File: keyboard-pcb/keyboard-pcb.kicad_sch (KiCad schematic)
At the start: 57 parts, among them SW1 SW_Push, SW10 SW_Push, SW11 SW_Push, SW12 SW_Push, SW13 SW_Push, SW14 SW_Push, SW15 SW_Push, SW16 SW_Push, SW17 SW_Push, SW18 SW_Push, SW19 SW_Push, SW2 SW_Push, SW20 SW_Push, SW21 SW_Push, SW22 SW_Push, SW23 SW_Push, SW24 SW_Push, SW25 SW_Push, SW26 SW_Push, SW27 SW_Push, SW28 SW_Push, SW3 SW_Push, SW4 SW_Push, SW5 SW_Push, SW6 SW_Push, SW7 SW_Push, SW8 SW_Push, SW9 SW_Push, U1 RC1602A

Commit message: placement in progress
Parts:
- removed D28: 1N914, Diode_THT:D_DO-35_SOD27_P7.62mm_Horizontal, symbol Diode:1N914
- removed SW28: SW_Push, Button_Switch_Keyboard:SW_Cherry_MX_1.00u_PCB, symbol Switch:SW_Push
- added U1: ATmega328-P, Package_DIP:DIP-28_W7.62mm, symbol MCU_Microchip_ATmega:ATmega328-P
- renumbered U1 to U2
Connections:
- net GND: now reaches U2.1 (VSS)
- net GND: now also U2.5 (R/W), U1.22 (GND), U1.8 (GND)
- net VCC: now reaches U2.2 (VDD)
- net VCC: now also U1.20 (AVCC), U1.7 (VCC)
- net ROW4: now reaches SW17.1, SW18.1, SW19.1, SW20.1
- net ROW4: now also U1.6 (PD4)
- net ROW5: now reaches SW21.1, SW22.1, SW23.1, SW24.1
- net ROW5: now also U1.11 (PD5)
- net COL1: now reaches D10.1 (K), D14.1 (K), D18.1 (K), D2.1 (K), D22.1 (K), D26.1 (K), D6.1 (K)
- net COL1: now also U1.27 (PC4)
- net ROW3: now reaches SW13.1, SW14.1, SW15.1, SW16.1
- net ROW3: now also U1.5 (PD3)
- net COL2: now reaches D11.1 (K), D15.1 (K), D19.1 (K), D23.1 (K), D27.1 (K), D3.1 (K), D7.1 (K)
- net COL2: now also U1.28 (PC5)
- net COL0: now reaches D1.1 (K), D13.1 (K), D17.1 (K), D21.1 (K), D25.1 (K), D5.1 (K), D9.1 (K)
- net COL0: now also U1.16 (PB2)
- net ROW0: now reaches SW1.1, SW2.1, SW3.1, SW4.1
- net ROW0: now also U1.2 (PD0)
- net ROW1: now reaches SW5.1, SW6.1, SW7.1, SW8.1
- net ROW1: now also U1.3 (PD1)
- net COL3: now reaches D12.1 (K), D16.1 (K), D20.1 (K), D24.1 (K), D4.1 (K), D8.1 (K)
- net COL3: now also U1.13 (PD7)
- net ROW2: now reaches SW10.1, SW11.1, SW12.1, SW9.1
- net ROW2: now also U1.4 (PD2)
- net ROW6: now reaches SW25.1, SW26.1, SW27.1
- net ROW6: now also U1.12 (PD6)
- new net D0: U1.23 (PC0)
- new net D1: U1.24 (PC1)
- new net D2: U1.25 (PC2)
- new net D3: U1.26 (PC3)
- new net EN: U1.9 (XTAL1/PB6)
- new net MISO: U1.18 (PB4)
- new net MOSI: U1.17 (PB3)
- new net RS: U1.10 (XTAL2/PB7)
- new net SCK: U1.19 (PB5)
- new net nRST: U1.1 (~{RESET}/PC6)
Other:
- company: (none) -> UPCO Graphics Systems
- title: (none) -> Hex Calculator
- moved on the sheet: D1, D10, D11, D12, D13, D14, D15, D16, D17, D18, D19, D2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

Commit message: placement
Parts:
- added R1: R, Resistor_THT:R_Axial_DIN0207_L6.3mm_D2.5mm_P7.62mm_Horizontal, symbol Device:R
- added RV1: R_Potentiometer, Potentiometer_THT:Potentiometer_Bourns_3266P_Horizontal, symbol Device:R_Potentiometer
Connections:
- net D0: now also U2.11 (DB4)
- net D1: now also U2.12 (DB5)
- net D2: now also U2.13 (DB6)
- net D3: now also U2.14 (DB7)
- net EN: now also U2.6 (E)
- net GND: now also U2.10 (DB3), U2.7 (DB0), U2.8 (DB1), U2.9 (DB2), R1.2, RV1.3
- net RS: now also U2.4 (RS)
- net VCC: now also U2.15 (A/VEE), RV1.1
- net at U2.16 (K): now also R1.1
- net at U2.3 (VO): now also RV1.2

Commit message: working on placement
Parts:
- added BT1: 2xAAA, symbol Device:Battery
- added C1, C3: 0.1uF, Capacitor_SMD:C_0805_2012Metric_Pad1.18x1.45mm_HandSolder, symbol Device:C
- added C2: 10uF, Capacitor_SMD:C_0805_2012Metric_Pad1.18x1.45mm_HandSolder, symbol Device:C
- added D1, D11, D2: LED, LED_THT:LED_D3.0mm, symbol Device:LED
- added J1: Conn_02x03_Odd_Even, Connector_PinHeader_2.54mm:PinHeader_2x03_P2.54mm_Vertical, symbol Connector_Generic:Conn_02x03_Odd_Even
- added R1, R2, R3: 470, Resistor_THT:R_Axial_DIN0207_L6.3mm_D2.5mm_P7.62mm_Horizontal, symbol Device:R
- added R4: 10k, Resistor_THT:R_Axial_DIN0207_L6.3mm_D2.5mm_P7.62mm_Horizontal, symbol Device:R
- added SW5: SW_SPST, Connector_PinHeader_2.54mm:PinHeader_1x02_P2.54mm_Vertical, symbol Switch:SW_SPST
- added U1: R1500H, Package_TO_SOT_SMD:SOT-89-5_Handsoldering, symbol R1500H_vreg:R1500H
- R5: renamed from R1; value R -> 470
- RV1: value R_Potentiometer -> 10k
- renumbered D8 to D10, D9 to D12, D10 to D13, D11 to D14, D12 to D15, D13 to D16, D14 to D17, D15 to D18, D16 to D19, D17 to D20, D18 to D21, D19 to D22, D20 to D23, D21 to D24, D22 to D25, D23 to D26, D24 to D27, D25 to D28, D26 to D29, D1 to D3, D27 to D30, D2 to D4, D3 to D5, D4 to D6, D5 to D7, D6 to D8, D7 to D9, SW9 to SW10, SW10 to SW11, SW11 to SW12, SW12 to SW13, SW13 to SW14, SW14 to SW15, SW15 to SW16, SW16 to SW17, SW17 to SW18, SW18 to SW19, SW19 to SW20, SW20 to SW21, SW21 to SW22, SW22 to SW23, SW23 to SW24, SW24 to SW25, SW25 to SW26, SW26 to SW27, SW27 to SW28, SW5 to SW6, SW6 to SW7, SW7 to SW8, SW8 to SW9, U1 to U2, U2 to U3
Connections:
- net GND: now also BT1.2 (-), C1.2, C2.2, C3.2, D11.1 (K), J1.6 (Pin_6), U1.2 (GND), U1.3 (GND)
- net MISO: now also J1.1 (Pin_1)
- net MOSI: now also J1.4 (Pin_4)
- net SCK: now also J1.3 (Pin_3)
- net VCC: now also C1.1, C2.1, J1.2 (Pin_2), R1.1, R2.1, R3.1, R4.1, U1.5 (VOUT)
- net nRST: now also J1.5 (Pin_5), R4.2
- net at U2.14 (PB0): now also D1.1 (K)
- net at U2.15 (PB1): now also D2.1 (K)
- new net: C3.1, SW5.1 (A), U1.1 (VIN), U1.4 (CE)
- new net: D11.2 (A), R3.2
- new net: D2.2 (A), R2.2
- new net: BT1.1 (+), SW5.2 (B)
- new net: D1.2 (A), R1.2

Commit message: starting software
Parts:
- BT1: footprint (none) -> Battery:BatteryHolder_Keystone_2468_2xAAA
- C1, C2, C3: footprint Capacitor_SMD:C_0805_2012Metric_Pad1.18x1.45mm_HandSolder -> Capacitor_THT:C_Disc_D5.0mm_W2.5mm_P2.50mm
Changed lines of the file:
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@@
       (effects (font (size 1.27 1.27)) (justify left))
     )
-    (property "Footprint" "Capacitor_SMD:C_0805_2012Metric_Pad1.18x1.45mm_HandSolder" (at 219.4052 68.58 0)
+    (property "Footprint" "Capacitor_THT:C_Disc_D5.0mm_W2.5mm_P2.50mm" (at 219.4052 68.58 0)
       (effects (font (size 1.27 1.27)) hide)
     )
@@
       (effects (font (size 1.27 1.27)) (justify left))
     )
-    (property "Footprint" "Capacitor_SMD:C_0805_2012Metric_Pad1.18x1.45mm_HandSolder" (at 256.2352 66.04 0)
+    (property "Footprint" "Capacitor_THT:C_Disc_D5.0mm_W2.5mm_P2.50mm" (at 256.2352 66.04 0)
       (effects (font (size 1.27 1.27)) hide)
     )
@@
       (effects (font (size 1.27 1.27)) (justify left))
     )
-    (property "Footprint" "" (at 204.47 63.246 90)
+    (property "Footprint" "Battery:BatteryHolder_Keystone_2468_2xAAA" (at 204.47 63.246 90)
       (effects (font (size 1.27 1.27)) hide)
     )
@@
       (effects (font (size 1.27 1.27)) (justify left))
     )
-    (property "Footprint" "Capacitor_SMD:C_0805_2012Metric_Pad1.18x1.45mm_HandSolder" (at 27.6352 27.94 0)
-      (effects (font (size 1.27 1.27)) hide)
-    )
+    (property "Footprint" "Capacitor_THT:C_Disc_D5.0mm_W2.5mm_P2.50mm" (at 27.6352 27.94 0)
+      (effects (font (size 1.27 1.27)) hide)
+    )

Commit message: placement done?
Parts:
- SW5: footprint Connector_PinHeader_2.54mm:PinHeader_1x02_P2.54mm_Vertical -> my_switch:ANT11TFHQE_switch; CatNo (none) -> 2449-ANT11TFHQE-ND
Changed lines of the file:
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@@
   )
   (symbol (lib_id "Switch:SW_SPST") (at 210.82 54.61 0) (mirror y) (unit 1)
-    (in_bom yes) (on_board yes) (dnp no) (fields_autoplaced)
-    (property "Reference" "SW5" (at 210.82 49.53 0)
+    (in_bom yes) (on_board yes) (dnp no)
+    (property "Reference" "SW5" (at 205.74 50.8 0)
       (effects (font (size 1.27 1.27)))
     )
-    (property "Value" "SW_SPST" (at 210.82 52.07 0)
+    (property "Value" "SW_SPST" (at 214.63 50.8 0)
       (effects (font (size 1.27 1.27)))
     )
-    (property "Footprint" "Connector_PinHeader_2.54mm:PinHeader_1x02_P2.54mm_Vertical" (at 210.82 54.61 0)
+    (property "Footprint" "my_switch:ANT11TFHQE_switch" (at 210.82 54.61 0)
       (effects (font (size 1.27 1.27)) hide)
     )
@@
       (effects (font (size 1.27 1.27)) hide)
     )
+    (property "CatNo" "2449-ANT11TFHQE-ND" (at 210.82 48.26 0)
+      (effects (font (size 1.27 1.27)))
+    )
     (pin "1")

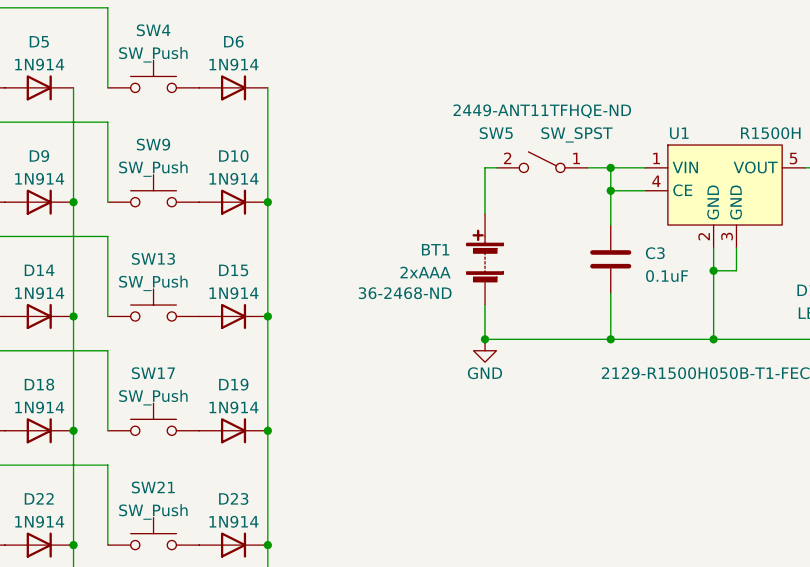
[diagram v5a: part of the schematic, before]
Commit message: change to AAA, software updates
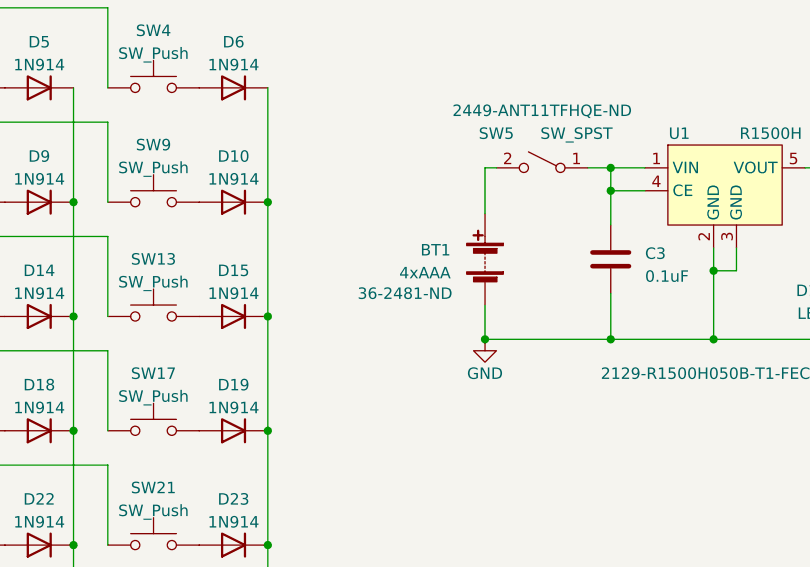
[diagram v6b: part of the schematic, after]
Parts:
- BT1: value 2xAAA -> 4xAAA; footprint Battery:BatteryHolder_Keystone_2468_2xAAA -> AAA_batt_holder:Keystone_4xAAA_2481; CatNo 36-2468-ND -> 36-2481-ND
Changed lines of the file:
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@@
       (effects (font (size 1.27 1.27)) (justify left))
     )
-    (property "Value" "2xAAA" (at 200.66 66.294 0)
+    (property "Value" "4xAAA" (at 200.66 66.294 0)
       (effects (font (size 1.27 1.27)) (justify left))
     )
-    (property "Footprint" "Battery:BatteryHolder_Keystone_2468_2xAAA" (at 204.47 63.246 90)
+    (property "Footprint" "AAA_batt_holder:Keystone_4xAAA_2481" (at 204.47 63.246 90)
       (effects (font (size 1.27 1.27)) hide)
     )
@@
       (effects (font (size 1.27 1.27)) hide)
     )
-    (property "CatNo" "36-2468-ND" (at 195.58 68.58 0)
+    (property "CatNo" "36-2481-ND" (at 195.58 68.58 0)
       (effects (font (size 1.27 1.27)))
     )

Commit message: V1 ready to order?
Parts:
- BT1: CatNo 36-2481-ND -> BC4AAAPC-ND
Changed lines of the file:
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@@
       (effects (font (size 1.27 1.27)) hide)
     )
-    (property "CatNo" "36-2481-ND" (at 195.58 68.58 0)
+    (property "CatNo" "BC4AAAPC-ND" (at 195.58 68.58 0)
       (effects (font (size 1.27 1.27)))
     )
